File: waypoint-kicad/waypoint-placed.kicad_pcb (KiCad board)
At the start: 2 copper layers, 62 x 42 mm, 83 parts, among them J1 USB_C_Receptacle_USB2.0_14P, J2 Conn_01x02, J3 Conn_Coaxial, J4 Conn_02x03_Odd_Even, J5 Conn_01x08, J6 Conn_01x02, Q1 NPN, SW1 SW_SPST, U1 nRF52840, U2 SX1262IMLTRT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

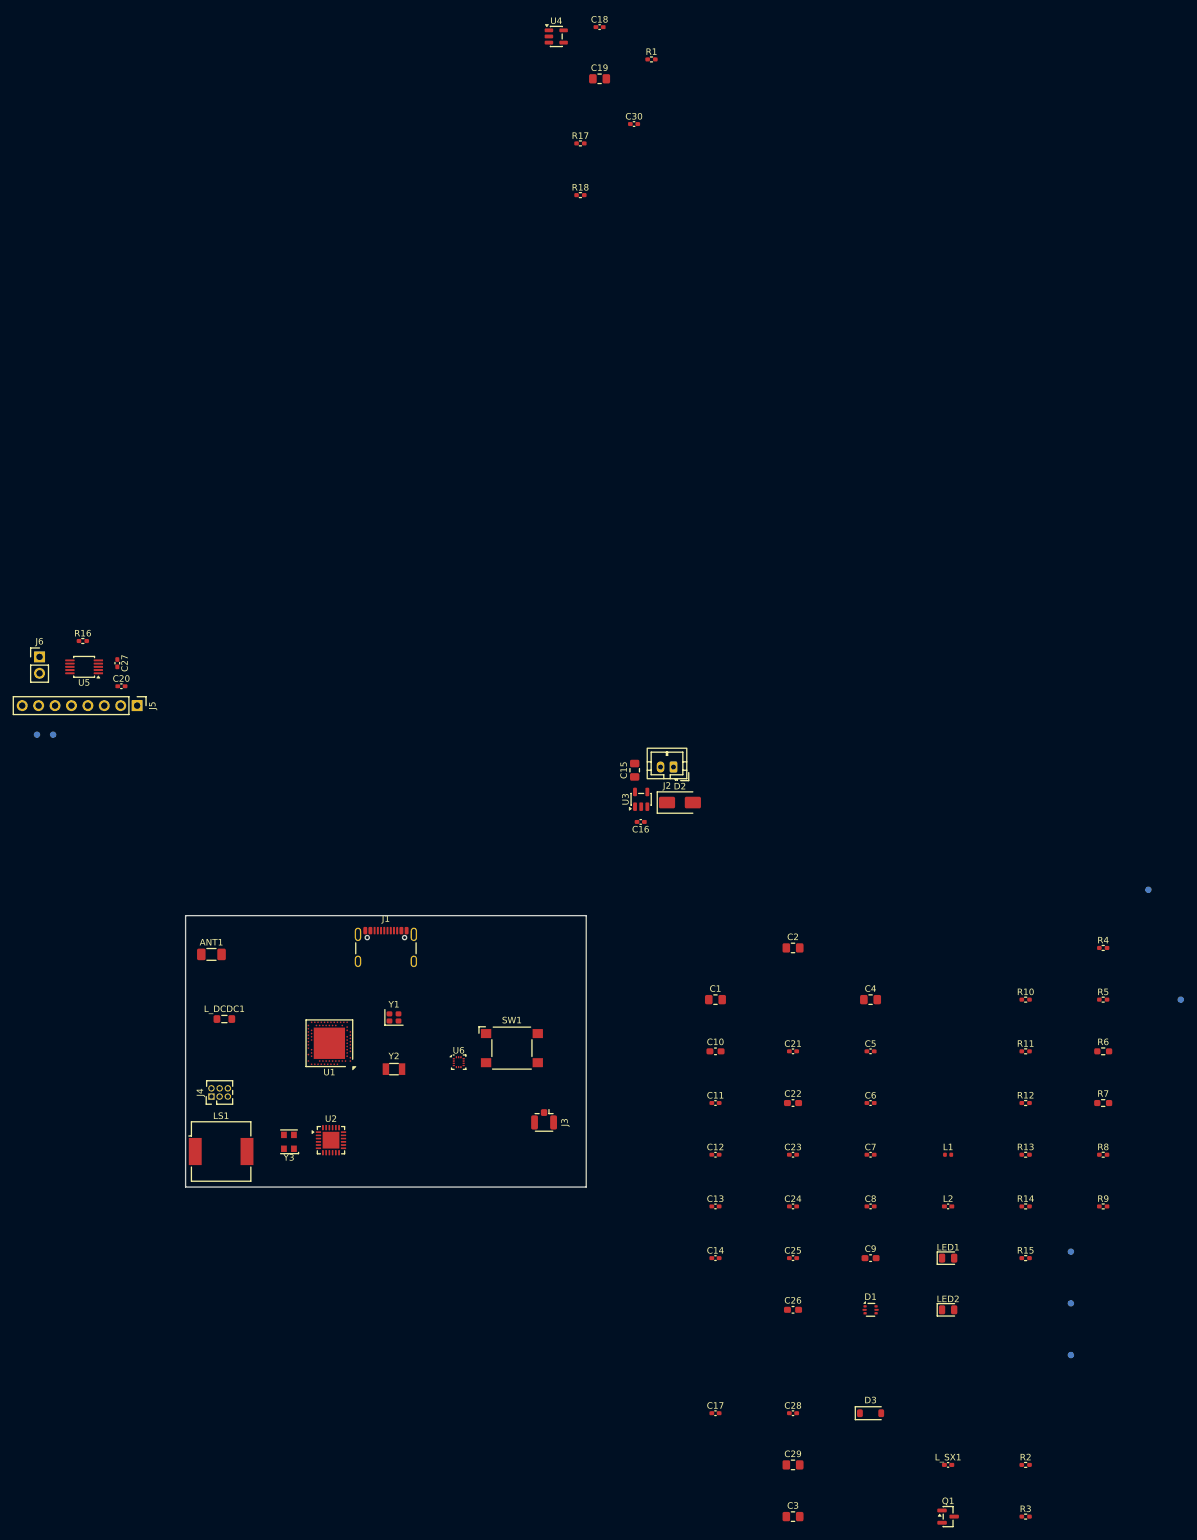
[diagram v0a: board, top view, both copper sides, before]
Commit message: Update documentation for waypoint-kicad: enhance component details and placements
- Added battery voltage divider components (R17, R18) to BOM and placement instructions.
- Corrected references for the accelerometer component from U7 to U6 in multiple documents.
- Revised resistor details in the schematic checklist to reflect the updated count and values.
- Updated component placement instructions to clarify the new configurations and connections.
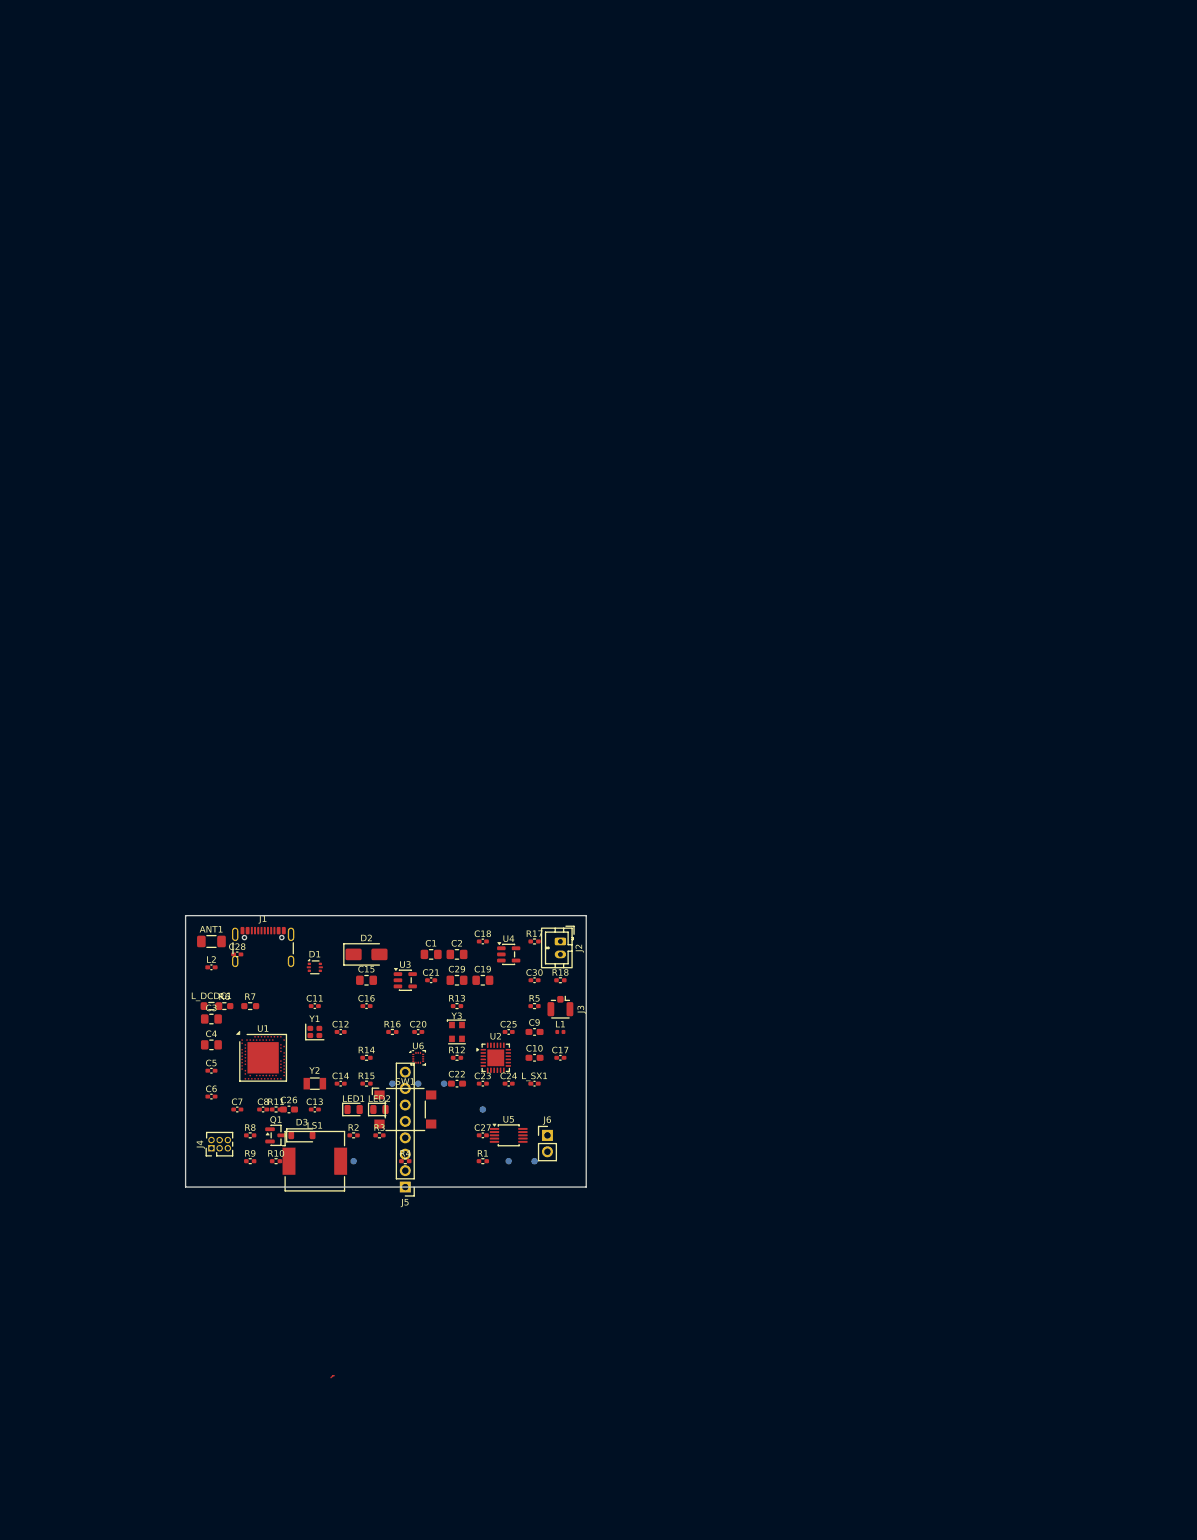
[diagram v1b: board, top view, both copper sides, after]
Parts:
- moved R1 172.5 mm to (46.0, 38.0)
- moved C18 142.6 mm to (46.0, 4.00)
- moved U4 142.2 mm to (50.0, 6.00)
- moved C19 140.7 mm to (46.0, 10.0)
- moved R6 136.2 mm to (6.00, 14.0)
- moved C30 133.4 mm to (54.0, 10.0)
- moved R7 132.8 mm to (10.0, 14.0)
- moved R9 132.2 mm to (10.0, 38.0)
- moved R8 132.0 mm to (10.0, 34.0)
- moved TP7 130.4 mm to (26.0, 38.0)
- moved R17 123.7 mm to (54.0, 4.00)
- moved R18 121.5 mm to (58.0, 10.0)
- moved L2 119.9 mm to (4.00, 8.00)
- moved Q1 119.6 mm to (14.0, 34.0)
- moved R10 118.7 mm to (14.0, 38.0)
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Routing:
- net /LRA_PLUS: track 0.00 -> 0.62 mm
